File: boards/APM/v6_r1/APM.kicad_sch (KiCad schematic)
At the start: 25 parts, among them J2 AUDIO_PWR, J4 LCD_display, J6 OSC_CTRL, J8 AUDIO_CTRL

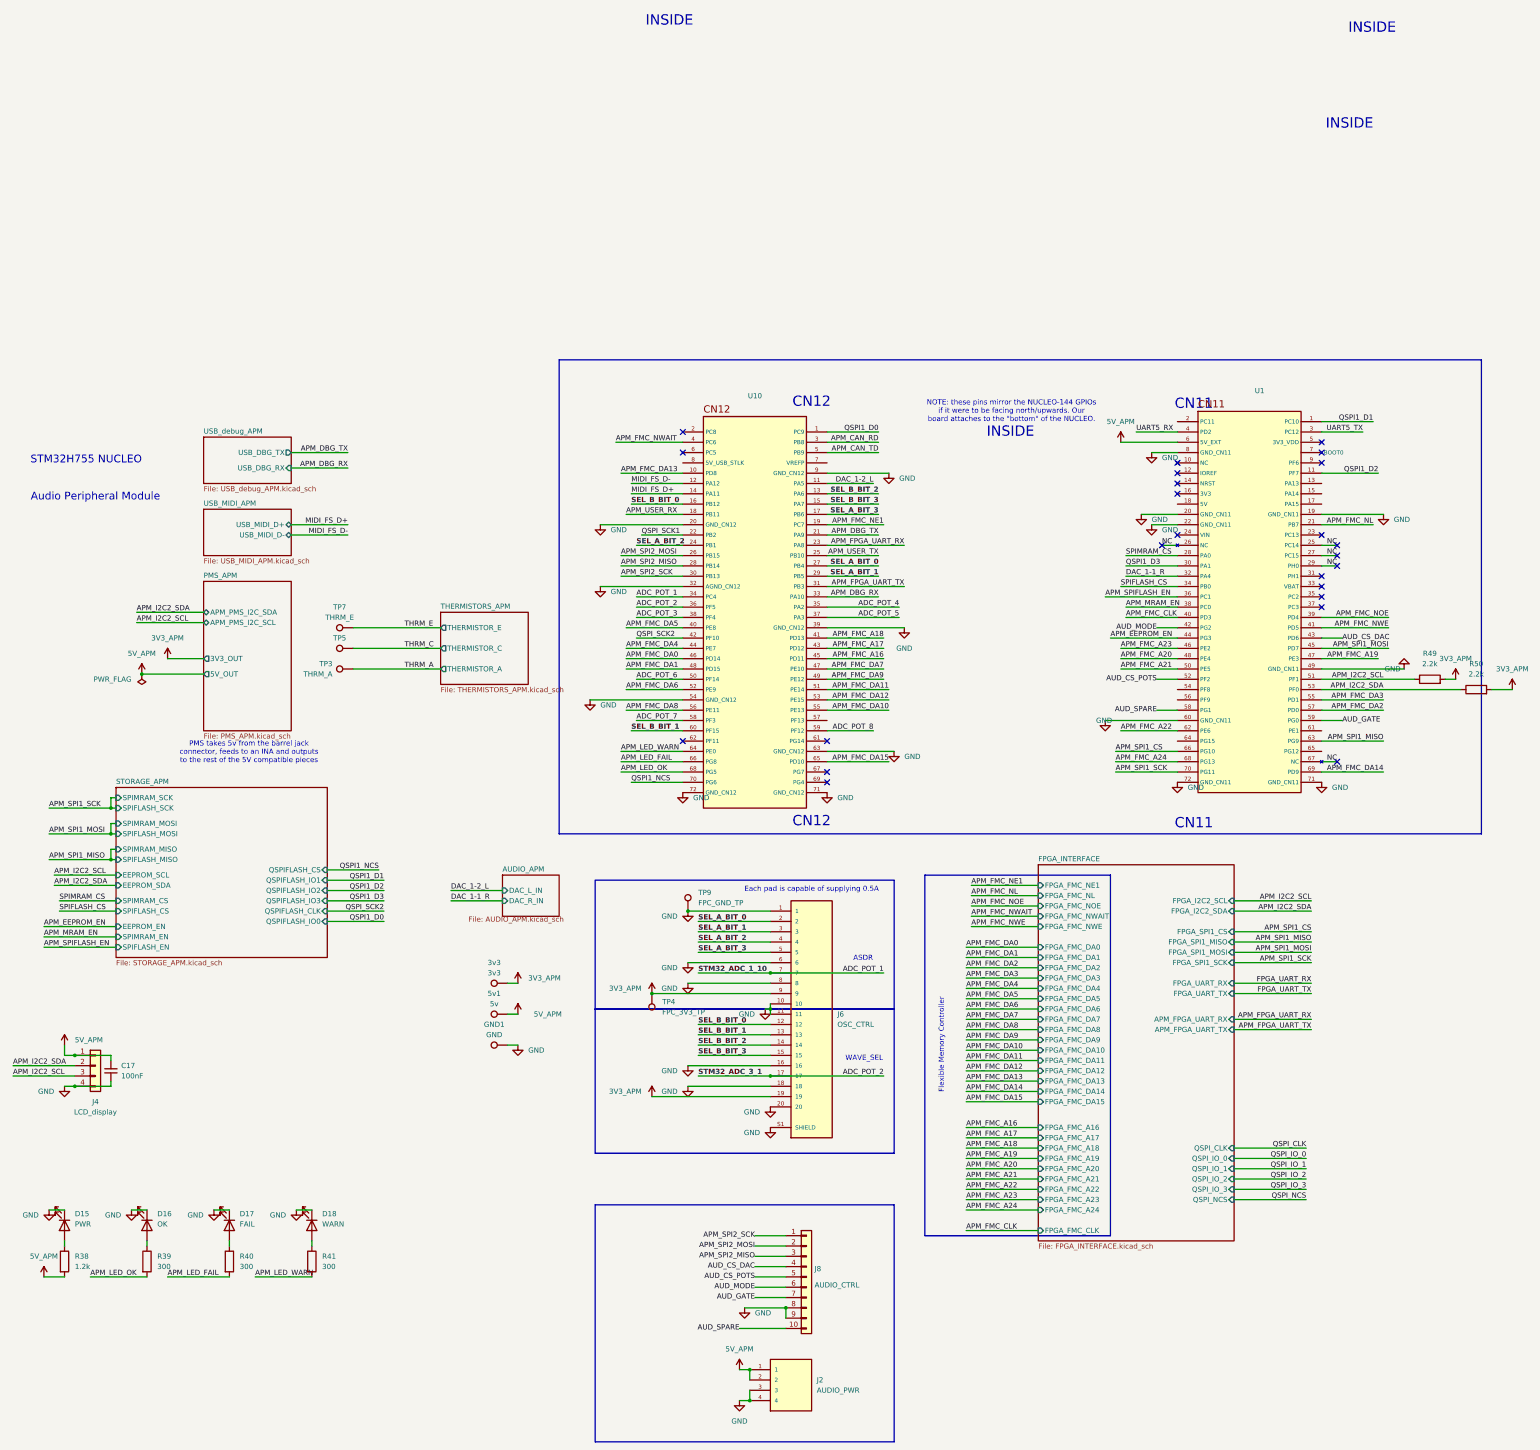
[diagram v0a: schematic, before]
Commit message: new APM board with ACM integrated. will need to really re-think layout and also form factor. mounting holes will be needed and likely standoffs for a nominal setting. i dont plan on making my own STM32H7 and gowin FPGA board for this, cost wise the dev board situation is better
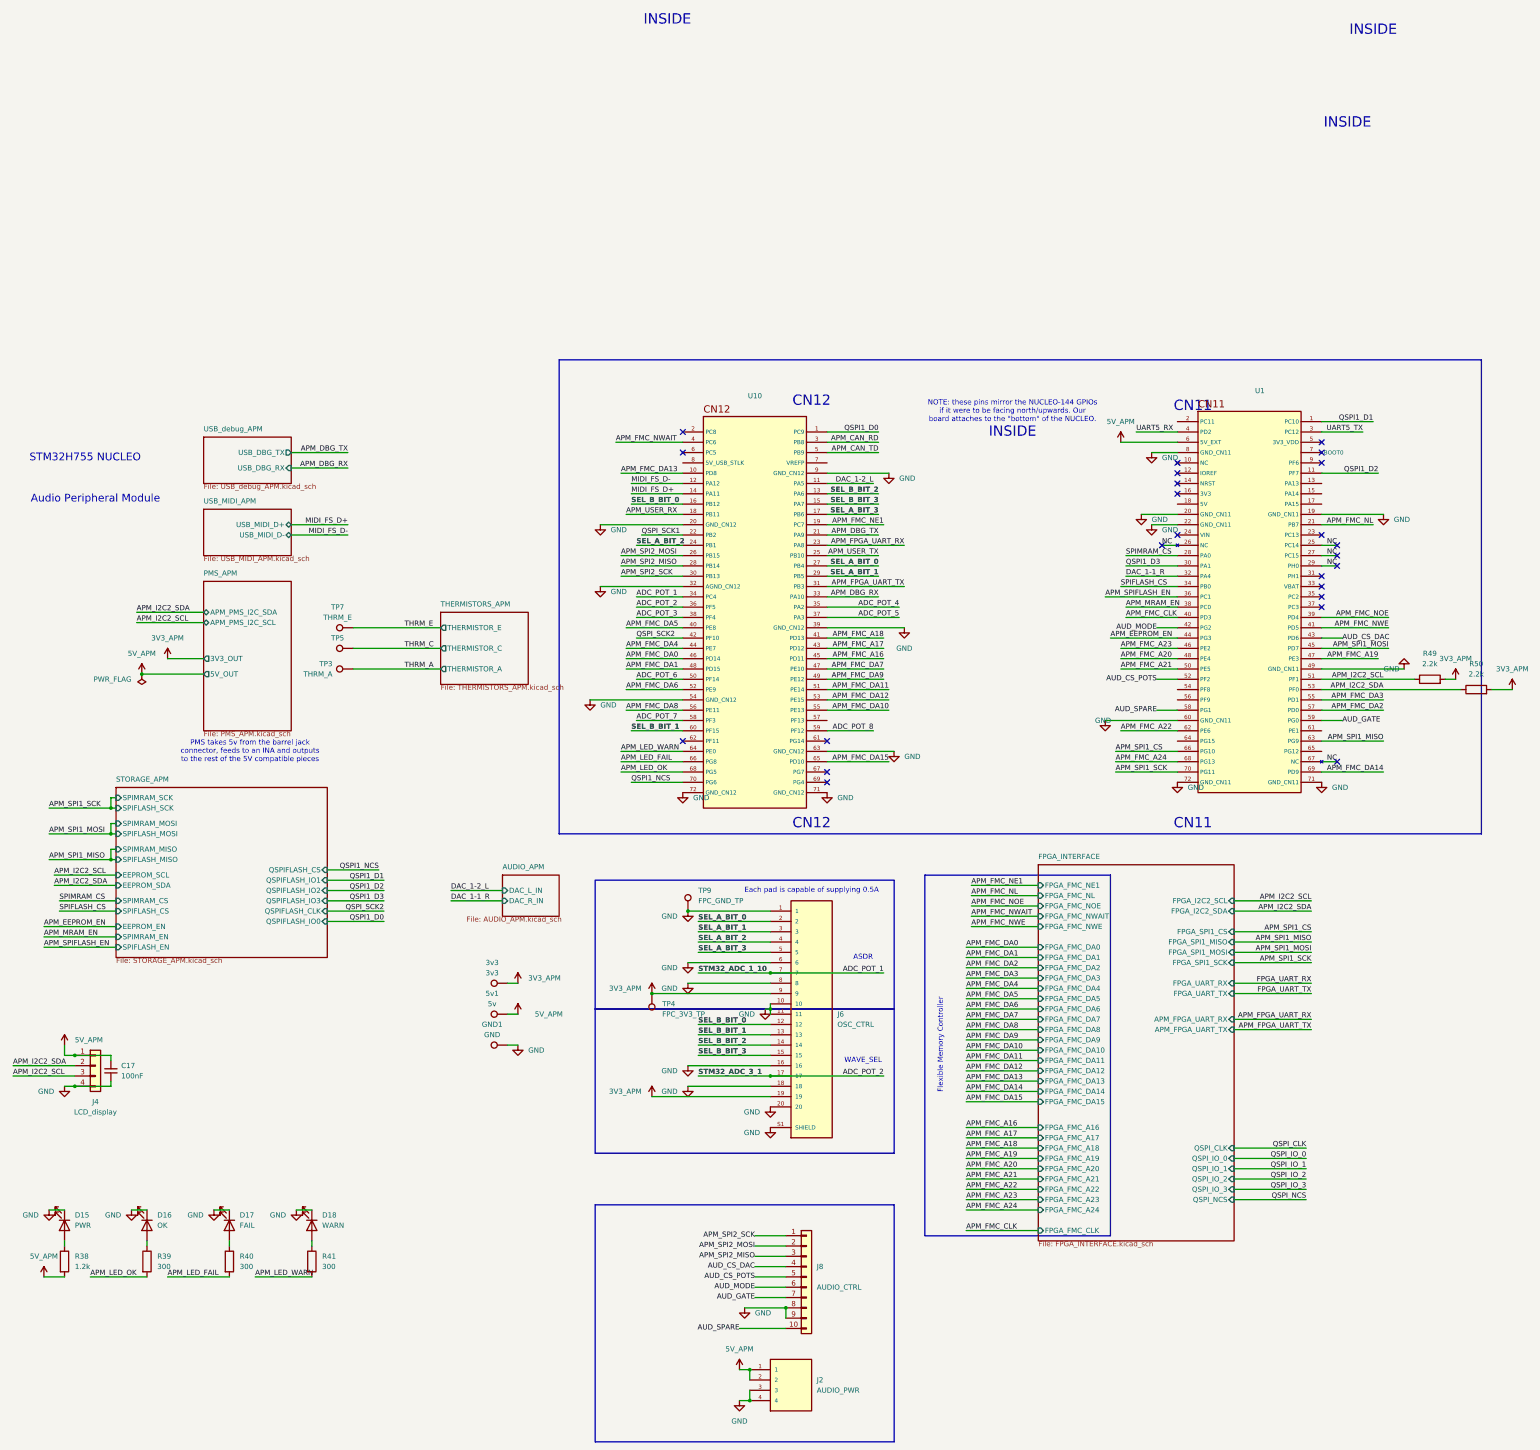
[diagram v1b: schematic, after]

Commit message: routing
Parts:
- removed 3v3: 3v3, TestPoint:TestPoint_Pad_D1.0mm, symbol Connector:TestPoint
- removed GND1: GND, TestPoint:TestPoint_Pad_D1.0mm, symbol Connector:TestPoint

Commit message: routed, dfc connector mixup?
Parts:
- added C25: 220uF 10V, Capacitor_SMD:CP_Elec_4x3, symbol Device:C_Small
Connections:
- net 5V_APM: now also C25.1
- net GND: now also C25.2
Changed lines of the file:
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@@
 	)
 	(junction
+		(at 203.2 265.43)
+		(diameter 0)
+		(color 0 0 0 0)
+	)
+	(junction
 		(at 210.82 168.91)
 		(diameter 0)
@@
 	)
 	(junction
+		(at 203.2 257.81)
+		(diameter 0)
+		(color 0 0 0 0)
+	)
+	(junction
 		(at 48.26 125.73)
 		(diameter 0)
@@
 	(wire
 		(pts
+			(xy 203.2 258.826) (xy 203.2 257.81)
+		)
+		(stroke
+			(width 0)
+			(type default)
+		)
+	)
+	(wire
+		(pts
 			(xy 346.71 36.83) (xy 360.68 36.83)
 		)
@@
 	(wire
 		(pts
+			(xy 189.738 263.906) (xy 203.2 263.906)
+		)
+		(stroke
+			(width 0)
+			(type default)
+		)
+	)
+	(wire
+		(pts
 			(xy 238.76 49.53) (xy 224.79 49.53)
 		)
@@
 	(wire
 		(pts
+			(xy 189.738 258.826) (xy 203.2 258.826)
+		)
+		(stroke
+			(width 0)
+			(type default)
+		)
+	)
+	(wire
+		(pts
 			(xy 173.99 59.69) (xy 189.23 59.69)
 		)
@@
 	(wire
 		(pts
+			(xy 203.2 263.906) (xy 203.2 265.43)
+		)
+		(stroke
+			(width 0)
+			(type default)
+		)
+	)
+	(wire
+		(pts
 			(xy 177.8 72.39) (xy 189.23 72.39)
 		)
@@
 					(unit 1)
 				)
+			)
+		)
+	)
+	(symbol
+		(lib_id "Device:C_Small")
+		(at 189.738 261.366 0)
+		(mirror y)
+		(unit 1)
+		(body_style 1)
+		(exclude_from_sim no)
+		(in_bom yes)
+		(on_board yes)
+		(in_pos_files yes)
+		(dnp no)
+		(fields_autoplaced yes)
+		(property "Reference" "C25"
+			(at 192.278 260.1022 0)
+			(show_name no)
+			(do_not_autoplace no)
+			(effects
+				(font
+					(size 1.27 1.27)
+				)
+				(justify right)
+			)
+		)
+		(property "Value" "220uF 10V"
+			(at 192.278 262.6422 0)
+			(show_name no)
+			(do_not_autoplace no)
+			(effects
+				(font
+					(size 1.27 1.27)
+				)
+				(justify right)
+			)
+		)
+		(property "Footprint" "Capacitor_SMD:CP_Elec_4x3"
+			(at 189.738 261.366 0)
+			(hide yes)
+			(show_name no)
+			(do_not_autoplace no)
+			(effects
+				(font
+					(size 1.27 1.27)
+				)
+			)
+		)
+		(property "Datasheet" ""
+			(at 189.738 261.366 0)
+			(hide yes)
+			(show_name no)
+			(do_not_autoplace no)
+			(effects
+				(font
+					(size 1.27 1.27)
+				)
+			)
+		)
+		(property "Description" "Unpolarized capacitor, small symbol"
+			(at 189.738 261.366 0)
+			(hide yes)
+			(show_name no)
+			(do_not_autoplace no)
+			(effects
+				(font
+					(size 1.27 1.27)
+				)
+			)
+		)
+		(pin "1"
+		)
+		(pin "2"
+		)
+		(instances
+			(project "APM"
+				(path "/63e257c1-2fa4-4533-ab9e-932d24befb8c"
+					(reference "C25")
+					(unit 1)
+				)
